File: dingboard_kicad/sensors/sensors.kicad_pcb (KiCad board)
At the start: 2 copper layers, 84.6 x 64 mm, 45 parts, among them J1 Bus_PCI_Express_x1, J2 TYPE-C-31-M-04, J3 Conn_01x02, U1 BNO055, U2 RP2040, U3 TPS2121RUXR, U4 W25Q128JVP, U5 BME680, U6 LMR51430 1.1k FPWM, U7 MCP25625-x-SS, X1 ABM8-272-T3

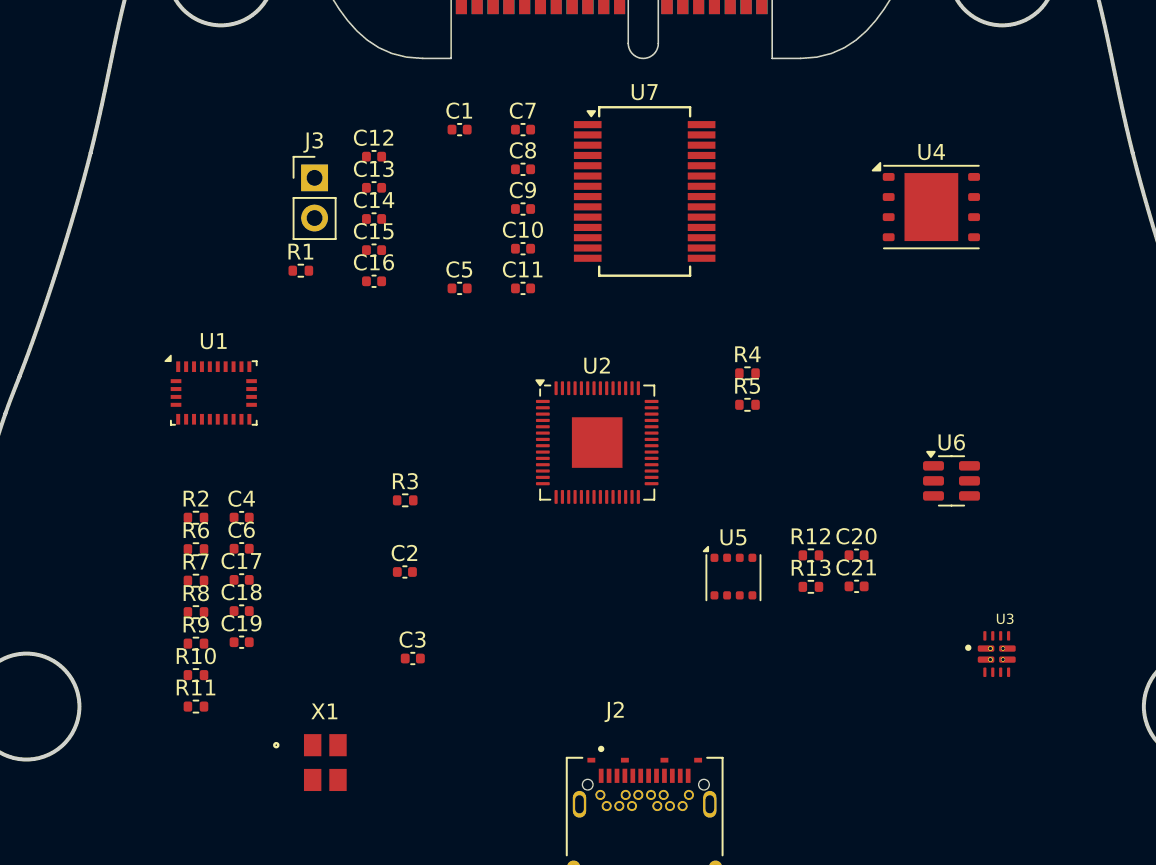
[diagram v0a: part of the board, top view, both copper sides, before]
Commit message: update BOM with new chip list
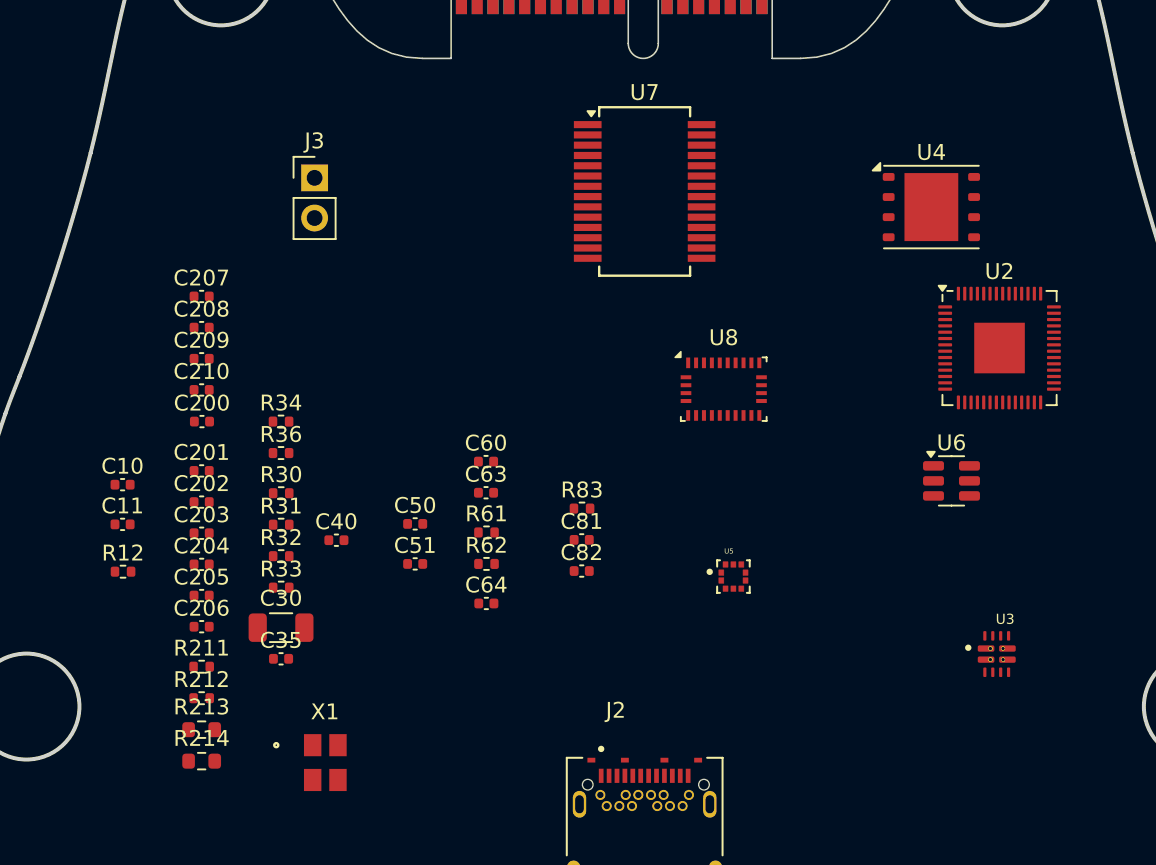
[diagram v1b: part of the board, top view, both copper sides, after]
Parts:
- removed C1, C12, C13, C14, C15, C16, C20, C21, C5, C7, C9: 100n, Capacitor_SMD:C_0402_1005Metric
- removed C17: 2.2u, Capacitor_SMD:C_0402_1005Metric
- removed C18: 0.1u, Capacitor_SMD:C_0402_1005Metric
- removed C19: 20uF / 25v, Capacitor_SMD:C_0402_1005Metric
- removed C2, C3: 15p, Capacitor_SMD:C_0402_1005Metric
- removed C4: 100u, Capacitor_SMD:C_0402_1005Metric
- removed C6: 0.01u, Capacitor_SMD:C_0402_1005Metric
- removed C8: 1u, Capacitor_SMD:C_0402_1005Metric
- removed R1, R3: 1k, Resistor_SMD:R_0402_1005Metric
- removed R10: 100k, Resistor_SMD:R_0402_1005Metric
- removed R11: 22.1k, Resistor_SMD:R_0402_1005Metric
- removed R13: 4.7k, Resistor_SMD:R_0402_1005Metric
- removed R2: 51.1k, Resistor_SMD:R_0402_1005Metric
- removed R4, R5: 27, Resistor_SMD:R_0402_1005Metric
- removed R6, R7, R8, R9: 23.7k, Resistor_SMD:R_0402_1005Metric
- removed U1: BNO055, Package_LGA:LGA-28_5.2x3.8mm_P0.5mm
- added C200: 100n, Capacitor_SMD:C_0402_1005Metric, F.Cu at (120.5, 92.0)
- added C201: 100n, Capacitor_SMD:C_0402_1005Metric, F.Cu at (120.5, 95.2)
- added C202: 100n, Capacitor_SMD:C_0402_1005Metric, F.Cu at (120.5, 97.1)
- added C203: 100n, Capacitor_SMD:C_0402_1005Metric, F.Cu at (120.5, 99.1)
- added C204: 100n, Capacitor_SMD:C_0402_1005Metric, F.Cu at (120.5, 101.1)
- added C205: 100n, Capacitor_SMD:C_0402_1005Metric, F.Cu at (120.5, 103.0)
- added C206: 100n, Capacitor_SMD:C_0402_1005Metric, F.Cu at (120.5, 105.0)
- added C207: 100n, Capacitor_SMD:C_0402_1005Metric, F.Cu at (120.5, 84.1)
- added C208: 100n, Capacitor_SMD:C_0402_1005Metric, F.Cu at (120.5, 86.1)
- added C209: 1u, Capacitor_SMD:C_0402_1005Metric, F.Cu at (120.5, 88.1)
- added C210: 1u, Capacitor_SMD:C_0402_1005Metric, F.Cu at (120.5, 90.0)
- added C30: 100u, Capacitor_SMD:C_1206_3216Metric, F.Cu at (125.5, 105.1)
- added C35: 0.01u, Capacitor_SMD:C_0402_1005Metric, F.Cu at (125.5, 107.0)
- added C40: 100n, Capacitor_SMD:C_0402_1005Metric, F.Cu at (129.0, 99.5)
- added C50: 100n, Capacitor_SMD:C_0402_1005Metric, F.Cu at (134.0, 98.5)
- added C51: 100n, Capacitor_SMD:C_0402_1005Metric, F.Cu at (134.0, 101.0)
- added C60: 100n, Capacitor_SMD:C_0402_1005Metric, F.Cu at (138.5, 94.6)
- added C63: 20uF / 25v, Capacitor_SMD:C_0402_1005Metric, F.Cu at (138.5, 96.5)
- added C64: 2.2u, Capacitor_SMD:C_0402_1005Metric, F.Cu at (138.5, 103.5)
- added C81: 100n, Capacitor_SMD:C_0402_1005Metric, F.Cu at (144.5, 99.5)
- added C82: 100n, Capacitor_SMD:C_0402_1005Metric, F.Cu at (144.5, 101.5)
- added R211: 4.7k, Resistor_SMD:R_0402_1005Metric, F.Cu at (120.5, 107.5)
- added R212: 4.7k, Resistor_SMD:R_0402_1005Metric, F.Cu at (120.5, 109.5)
- added R213: 27, Resistor_SMD:R_0603_1608Metric, F.Cu at (120.5, 111.5)
- added R214: 27, Resistor_SMD:R_0603_1608Metric, F.Cu at (120.5, 113.5)
- added R30: 1k, Resistor_SMD:R_0402_1005Metric, F.Cu at (125.5, 96.6)
- added R31: 23.7k, Resistor_SMD:R_0402_1005Metric, F.Cu at (125.5, 98.6)
- added R32: 23.7k, Resistor_SMD:R_0402_1005Metric, F.Cu at (125.5, 100.6)
- added R33: 23.7k, Resistor_SMD:R_0402_1005Metric, F.Cu at (125.5, 102.5)
- added R34: 23.7k, Resistor_SMD:R_0402_1005Metric, F.Cu at (125.5, 92.0)
- added R36: 51.1k, Resistor_SMD:R_0402_1005Metric, F.Cu at (125.5, 94.0)
- added R61: 100k, Resistor_SMD:R_0402_1005Metric, F.Cu at (138.5, 99.1)
- added R62: 22.1k, Resistor_SMD:R_0402_1005Metric, F.Cu at (138.5, 101.0)
- added R83: 10k, Resistor_SMD:R_0402_1005Metric, F.Cu at (144.5, 97.5)
- added U8: BNO055, Package_LGA:LGA-28_5.2x3.8mm_P0.5mm, F.Cu at (153.5, 90.0)
- C10: value 1u -> 15p
- C11: value 100n -> 15p
- R12: value 4.7k -> 1k
- U5: value BME680 -> BMP388; footprint Package_LGA:Bosch_LGA-8_3x3mm_P0.8mm_ClockwisePinNumbering -> BMP388:PQFN50P200X200X80-10N
- moved R12 43.5 mm to (115.5, 101.5)
- moved C10 29.4 mm to (115.5, 96.0)
- moved C11 29.4 mm to (115.5, 98.5)
- moved U2 26.1 mm to (170.9, 87.4)
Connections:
- C10 pad 1: +3V3 -> /XIN
- C11 pad 1: +3V3 -> Net-(C11-Pad1)
- R12 pad 1: +3V3 -> /XOUT
- R12 pad 2: SDA -> Net-(C11-Pad1)
- U2 pad 5: unconnected-(U2-GPIO3-Pad5) -> BMPINT
- U2 pad 7: unconnected-(U2-GPIO5-Pad7) -> BNOINT
- U2 pad 9: unconnected-(U2-GPIO7-Pad9) -> BNORESET
- U4 pad 4: unconnected-(U4-GND-Pad4) -> GND
- U5 pad 1: GND -> +3.3V
- U5 pad 2: +3V3 -> SCL
- U5 pad 3: SDA -> GND
- U5 pad 4: SCL -> SDA
- U5 pad 6: +3V3 -> +3.3V
- U5 pad 7: GND -> BMPINT
- U5 pad 8: +3V3 -> GND
- X1 pad 3: Net-(C3-Pad1) -> Net-(C11-Pad1)

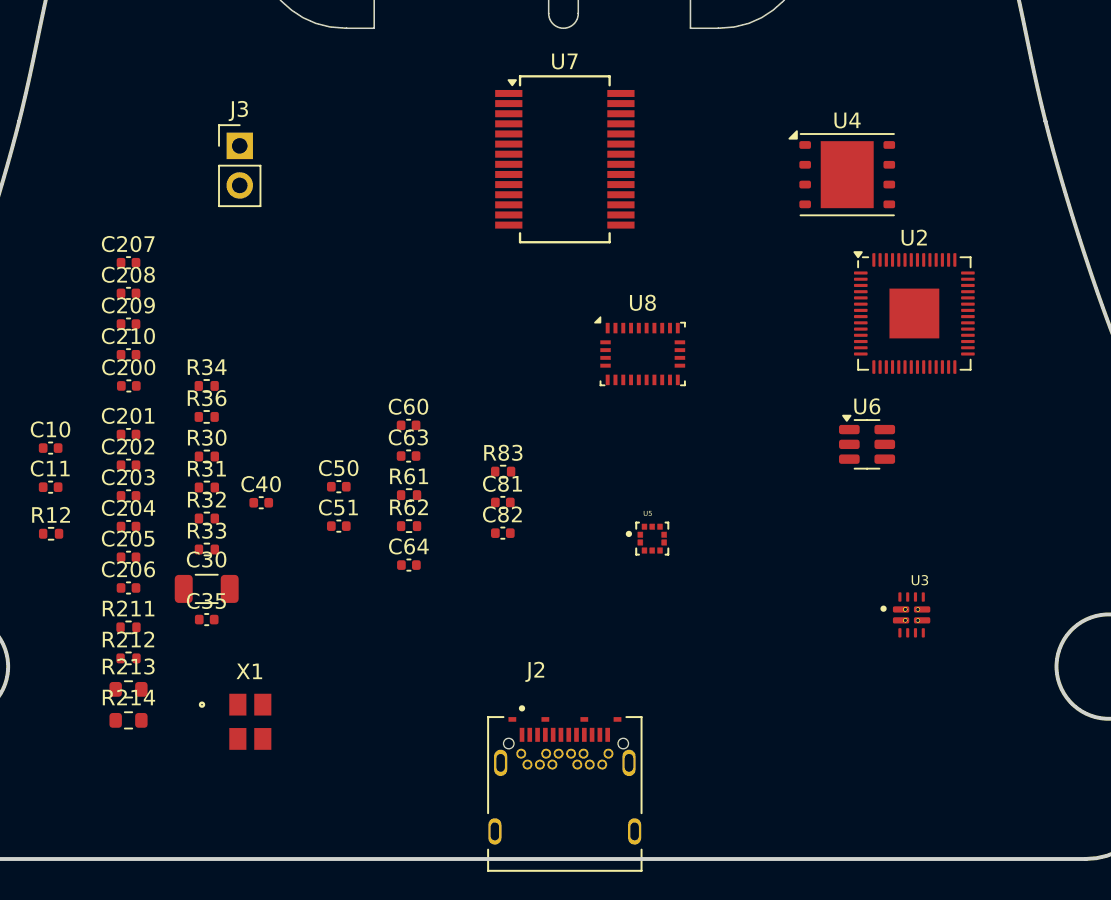
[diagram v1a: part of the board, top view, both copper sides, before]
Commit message: update BNO055 schematic
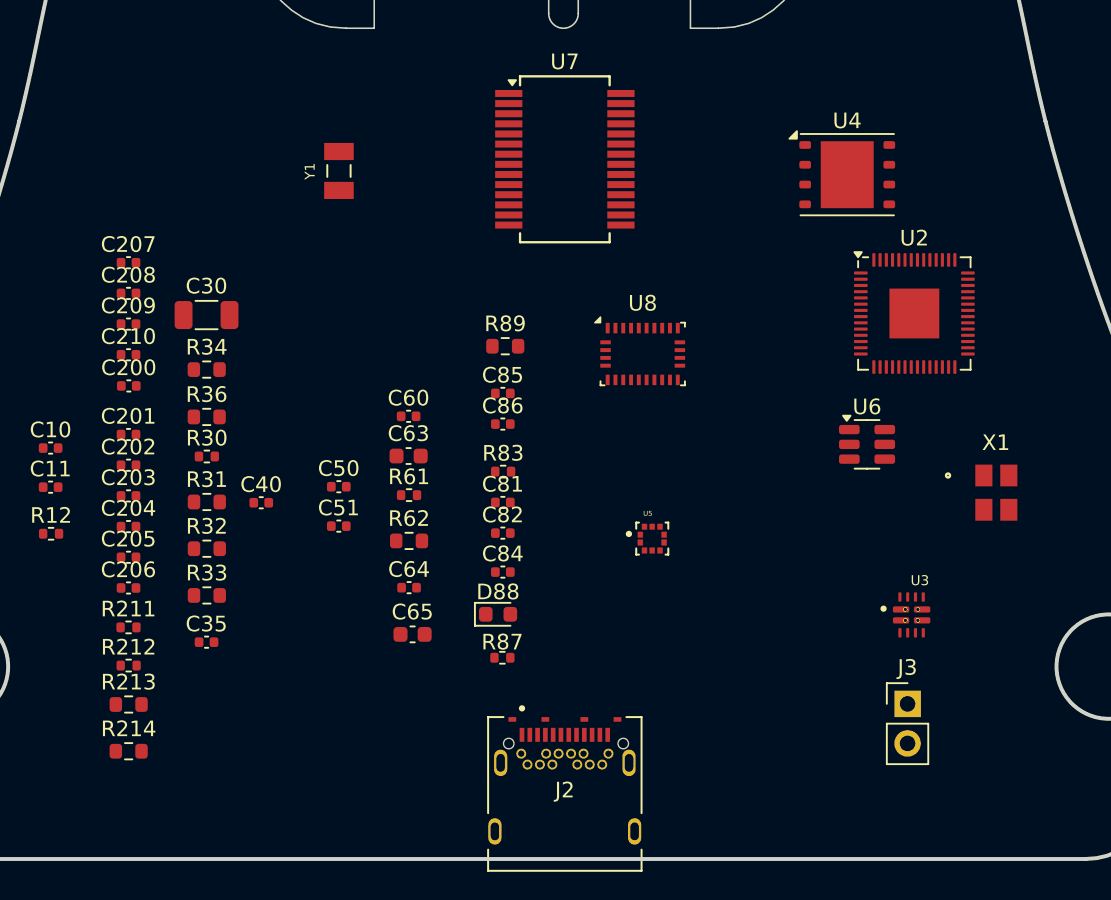
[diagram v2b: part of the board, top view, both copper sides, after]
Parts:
- added C65: 10uF / 25v, Capacitor_SMD:C_0603_1608Metric, F.Cu at (138.7, 108.0)
- added C84: 1u, Capacitor_SMD:C_0402_1005Metric, F.Cu at (144.5, 104.0)
- added C85: 22p, Capacitor_SMD:C_0402_1005Metric, F.Cu at (144.5, 92.5)
- added C86: 22p, Capacitor_SMD:C_0402_1005Metric, F.Cu at (144.5, 94.5)
- added D88: LED, LED_SMD:LED_0603_1608Metric, F.Cu at (144.2, 106.7)
- added R87: 10k, Resistor_SMD:R_0402_1005Metric, F.Cu at (144.5, 109.5)
- added R89: 150, Resistor_SMD:R_0603_1608Metric, F.Cu at (144.7, 89.5)
- added Y1: ABS07-32.768KHZ-T, ABS07-32.768KHZ-T:XTAL_ABS07-32.768KHZ-T, F.Cu at (134.0, 78.2)
- C63: value 20uF / 25v -> 10uF / 25v; footprint Capacitor_SMD:C_0402_1005Metric -> Capacitor_SMD:C_0603_1608Metric
- R31, R32, R33, R34, R36, R62: footprint Resistor_SMD:R_0402_1005Metric -> Resistor_SMD:R_0603_1608Metric
- moved J3 55.9 mm to (170.5, 112.5)
- moved X1 50.1 mm to (176.2, 98.9)
- moved C30 17.6 mm to (125.5, 87.5)
- moved R33 2.95 mm to (125.5, 105.5)
- moved R214 1.98 mm to (120.5, 115.5)
- moved R32 1.94 mm to (125.5, 102.5)
- moved C35 1.45 mm to (125.5, 108.5)
- moved C64 1.45 mm to (138.5, 105.0)
- moved R34 1.05 mm to (125.5, 91.0)
- moved R213 0.97 mm to (120.5, 112.5)
- moved R62 0.95 mm to (138.5, 102.0)
- moved R31 0.93 mm to (125.5, 99.5)
- moved C60 0.58 mm to (138.5, 94.0)
- moved R212 0.46 mm to (120.5, 110.0)
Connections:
- U2 pad 12: unconnected-(U2-GPIO9-Pad12) -> BOOT_LOAD
- U8 pad 10: unconnected-(U8-BL_IND-Pad10) -> Net-(D88-A)
- U8 pad 26: unconnected-(U8-XOUT32-Pad26) -> Net-(U8-XOUT32)
- U8 pad 27: unconnected-(U8-XIN32-Pad27) -> Net-(U8-XIN32)
- U8 pad 4: +3V3 -> BOOT_LOAD
- U8 pad 9: unconnected-(U8-CAP-Pad9) -> Net-(U8-CAP)

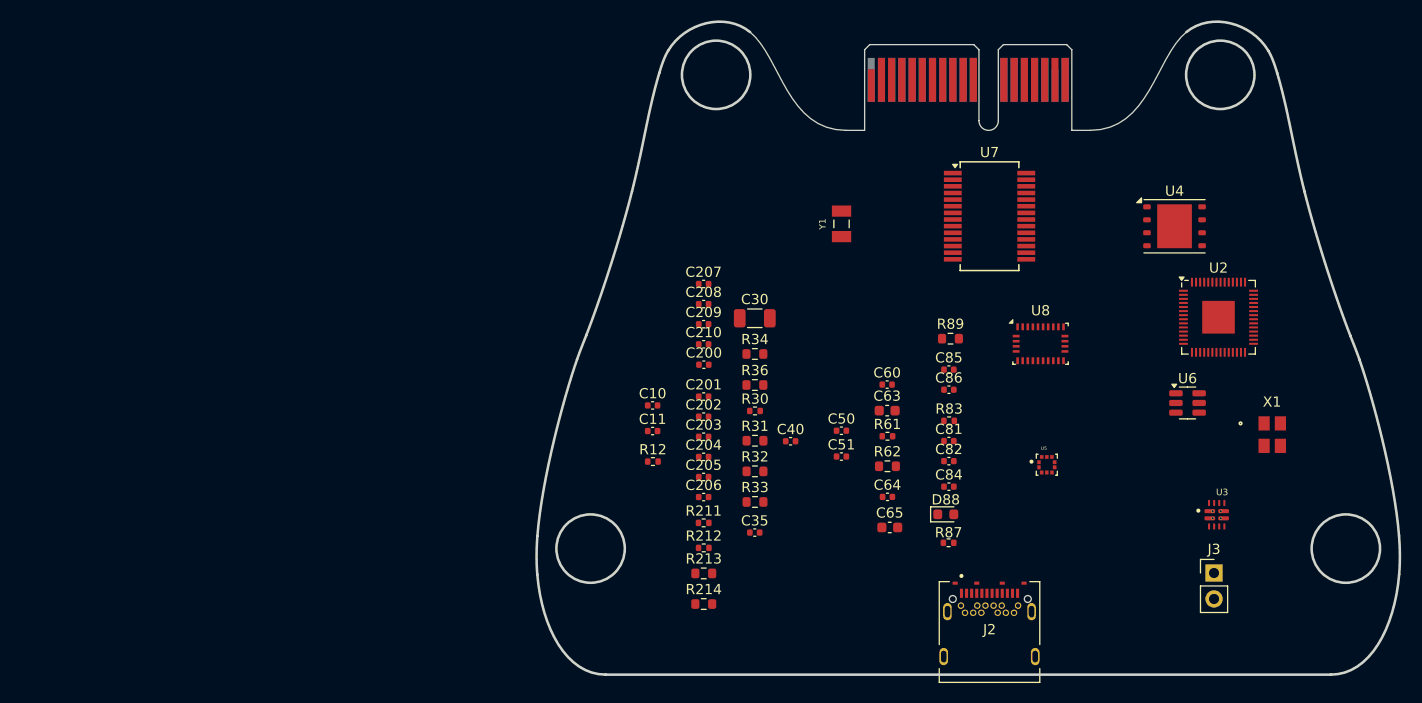
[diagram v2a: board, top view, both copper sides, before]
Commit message: add 5v buck-boost for CAN chip
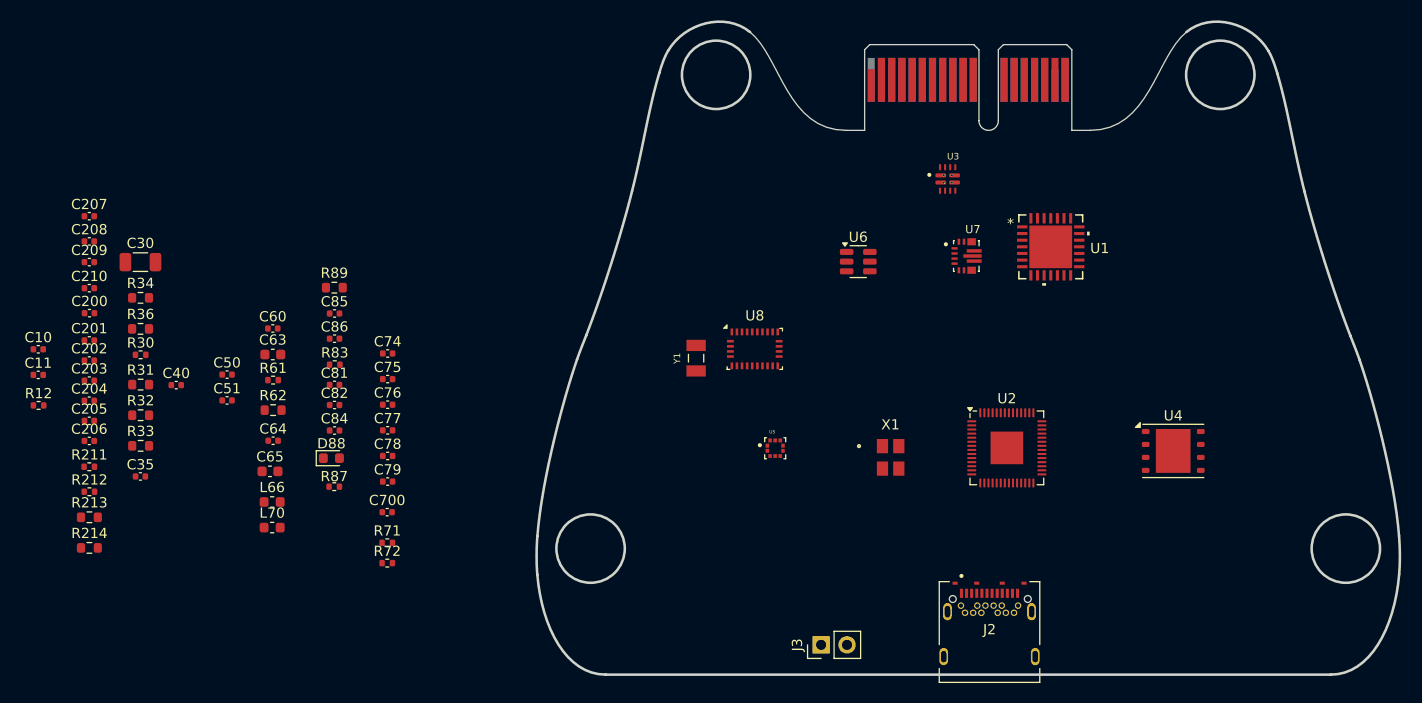
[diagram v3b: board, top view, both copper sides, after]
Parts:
- added C700: 10u, Capacitor_SMD:C_0402_1005Metric, F.Cu at (89.5, 106.5)
- added C74: 10uF, Capacitor_SMD:C_0402_1005Metric, F.Cu at (89.5, 91.0)
- added C75: 10uF, Capacitor_SMD:C_0402_1005Metric, F.Cu at (89.5, 93.5)
- added C76: 10uF, Capacitor_SMD:C_0402_1005Metric, F.Cu at (89.5, 96.0)
- added C77: 22u, Capacitor_SMD:C_0402_1005Metric, F.Cu at (89.5, 98.5)
- added C78: 22u, Capacitor_SMD:C_0402_1005Metric, F.Cu at (89.5, 101.0)
- added C79: 22u, Capacitor_SMD:C_0402_1005Metric, F.Cu at (89.5, 103.5)
- added L66: 2.2u, Inductor_SMD:L_0603_1608Metric, F.Cu at (78.2, 105.5)
- added L70: 1.5u, Inductor_SMD:L_0603_1608Metric, F.Cu at (78.2, 108.0)
- added R71: 10k, Resistor_SMD:R_0402_1005Metric, F.Cu at (89.5, 109.5)
- added R72: 100k, Resistor_SMD:R_0402_1005Metric, F.Cu at (89.5, 111.5)
- added U1: MCP25625T-E/ML, MCP25625:QFN28_6X6MC_MCH, F.Cu at (154.5, 80.5)
- C63, C65: value 10uF / 25v -> 10uF/25v
- R32, R34: value 23.7k -> 5k
- U7: value MCP25625-x-SS -> TPS63070RNMR; footprint Package_SO:SSOP-28_5.3x10.2mm_P0.65mm -> TPS63070RNMR:VREG_TPS63070RNMR
- moved C65 61.0 mm to (78.0, 102.5)
- moved R89 60.6 mm to (84.3, 84.5)
- moved C207 60.6 mm to (60.3, 77.5)
- moved C208 60.5 mm to (60.3, 80.0)
- moved C209 60.5 mm to (60.3, 82.0)
- moved C50 60.4 mm to (73.8, 93.0)
- moved C51 60.4 mm to (73.8, 95.5)
- moved C81 60.4 mm to (84.3, 94.0)
- moved C82 60.4 mm to (84.3, 96.0)
- moved C84 60.4 mm to (84.3, 98.5)
- moved C85 60.4 mm to (84.3, 87.0)
- moved D88 60.4 mm to (84.0, 101.2)
- moved R34 60.4 mm to (65.3, 85.5)
- moved R36 60.4 mm to (65.3, 88.5)
- moved R87 60.4 mm to (84.3, 104.0)
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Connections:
- C30 pad 1: /vpre -> vpre
- C60 pad 2: +3.3V -> Net-(U6-SW)
- C64 pad 1: /vpre -> vpre
- U3 pad 1: /vpre -> vpre
- U3 pad 1_1: /vpre -> vpre
- U3 pad 8: /vpre -> vpre
- U3 pad 8_1: /vpre -> vpre
- U6 pad 2: +3.3V -> Net-(U6-SW)
- U6 pad 3: /vpre -> vpre
- U6 pad 5: /vpre -> vpre
- U7 pad 1: unconnected-(U7-VIO-Pad1) -> Net-(U7-EN)
- U7 pad 10: unconnected-(U7-GND-Pad10) -> GND
- U7 pad 11: unconnected-(U7-~{Rx1BF}-Pad11) -> Net-(U7-L1)
- U7 pad 14: unconnected-(U7-SCK-Pad14) -> Net-(U7-EN)
- U7 pad 15: unconnected-(U7-SI-Pad15) -> GND
- U7 pad 2: unconnected-(U7-NC-Pad2) -> Net-(U7-PG)
- U7 pad 3: unconnected-(U7-CANL-Pad3) -> Net-(U7-VAUX)
- U7 pad 4: unconnected-(U7-CANH-Pad4) -> GND
- U7 pad 5: unconnected-(U7-STBY-Pad5) -> +5V
- U7 pad 6: unconnected-(U7-~{Tx1RTS}-Pad6) -> GND
- U7 pad 9: unconnected-(U7-OSC1-Pad9) -> Net-(U7-L2)
